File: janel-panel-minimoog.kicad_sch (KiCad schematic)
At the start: 2 parts, among them J2 Conn_01x03_Pin, J3 Conn_01x01_Pin

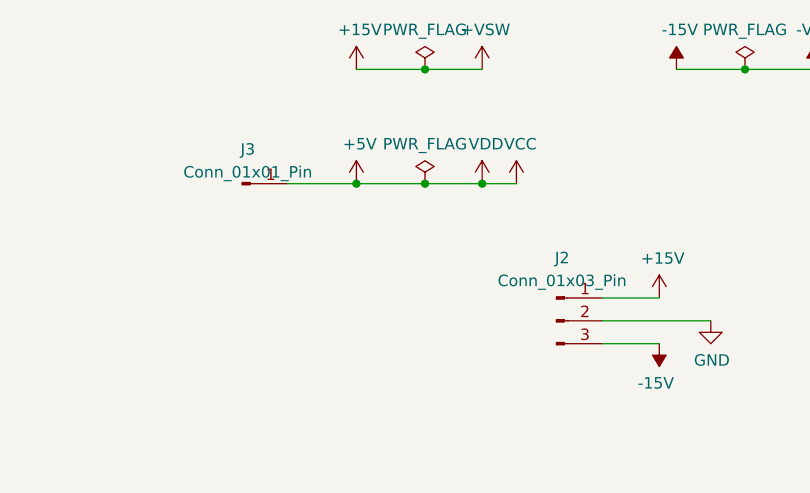
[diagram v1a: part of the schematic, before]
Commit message: Replace symbols with new library
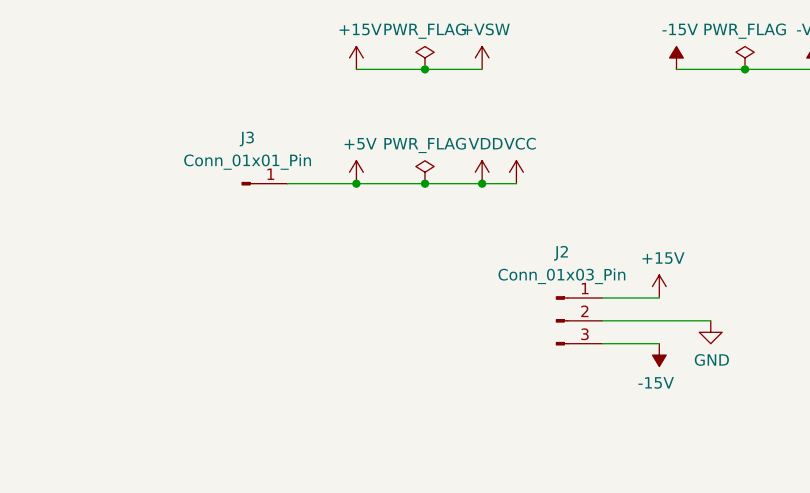
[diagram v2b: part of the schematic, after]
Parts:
- J2: footprint Connector_PinHeader_2.54mm:PinHeader_1x03_P2.54mm_Vertical -> (none)
- J3: footprint Connector_PinHeader_2.54mm:PinHeader_1x01_P2.54mm_Vertical -> (none)
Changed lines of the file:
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@@
 			)
 		)
-		(property "Description" ""
+		(property "Description" "Power symbol creates a global label with name \"+15V\""
 			(at 204.47 26.67 0)
 			(effects
@@
 					(size 1.27 1.27)
 				)
+				(hide yes)
 			)
 		)
@@
 			)
 		)
-		(property "Description" ""
+		(property "Description" "Power symbol creates a global label with name \"-15V\""
 			(at 240.03 26.67 0)
 			(effects
@@
 					(size 1.27 1.27)
 				)
+				(hide yes)
 			)
 		)
@@
 			)
 		)
-		(property "Description" ""
+		(property "Description" "Special symbol for telling ERC where power comes from"
 			(at 212.09 26.67 0)
 			(effects
@@
 					(size 1.27 1.27)
 				)
+				(hide yes)
 			)
 		)
@@
 			)
 		)
-		(property "Description" ""
+		(property "Description" "Special symbol for telling ERC where power comes from"
 			(at 247.65 26.67 0)
 			(effects
@@
 					(size 1.27 1.27)
 				)
+				(hide yes)
 			)
 		)
@@
 			)
 		)
-		(property "Description" ""
+		(property "Description" "Special symbol for telling ERC where power comes from"
 			(at 270.51 26.67 0)
 			(effects
@@
 					(size 1.27 1.27)
 				)
+				(hide yes)
 			)
 		)
@@
 			)
 		)
-		(property "Description" ""
+		(property "Description" "Power symbol creates a global label with name \"GND\" , ground"
 			(at 265.43 26.67 0)
 			(effects
@@
 					(size 1.27 1.27)
 				)
+				(hide yes)
 			)
 		)
@@
 			)
 		)
-		(property "Description" ""
+		(property "Description" "Power symbol creates a global label with name \"+VSW\""
 			(at 218.44 26.67 0)
 			(effects
@@
 					(size 1.27 1.27)
 				)
+				(hide yes)
 			)
 		)
@@
 			)
 		)
-		(property "Description" ""
+		(property "Description" "Power symbol creates a global label with name \"-VSW\""
 			(at 255.27 26.67 0)
 			(effects
@@
 					(size 1.27 1.27)
 				)
+				(hide yes)
 			)
 		)
@@
 			)
 		)
-		(property "Description" ""
+		(property "Description" "Power symbol creates a global label with name \"+5V\""
 			(at 204.47 39.37 0)
 			(effects
@@
 					(size 1.27 1.27)
 				)
+				(hide yes)
 			)
 		)
@@
 			)
 		)
-		(property "Description" ""
+		(property "Description" "Special symbol for telling ERC where power comes from"
 			(at 212.09 39.37 0)
 			(effects
@@
 					(size 1.27 1.27)
 				)
+				(hide yes)
 			)
 		)
@@
 			)
 		)
-		(property "Description" ""
+		(property "Description" "Power symbol creates a global label with name \"VDD\""
 			(at 218.44 39.37 0)
 			(effects
@@
 					(size 1.27 1.27)
 				)
+				(hide yes)
 			)
 		)
@@
 			)
 		)
-		(property "Description" ""
+		(property "Description" "Power symbol creates a global label with name \"VSS\""
 			(at 276.86 26.67 0)
 			(effects
@@
 					(size 1.27 1.27)
 				)
+				(hide yes)
 			)
 		)
@@
 			)
 		)
-		(property "Description" ""
+		(property "Description" "Power symbol creates a global label with name \"VCC\""
 			(at 222.25 39.37 0)
 			(effects
@@
 					(size 1.27 1.27)
 				)
+				(hide yes)
 			)
 		)
@@
 			)
 		)
-		(property "Description" ""
+		(property "Description" "Power symbol creates a global label with name \"GNDREF\" , reference supply ground"
 			(at 274.32 26.67 0)
 			(effects
@@
 					(size 1.27 1.27)
 				)
+				(hide yes)
 			)
 		)
@@
 			)
 		)
-		(property "Description" ""
+		(property "Description" "Power symbol creates a global label with name \"+15V\""
 			(at 238.125 52.07 0)
 			(effects
@@
 					(size 1.27 1.27)
 				)
+				(hide yes)
 			)
 		)
@@
 			)
 		)
-		(property "Description" ""
+		(property "Description" "Power symbol creates a global label with name \"-15V\""
 			(at 238.125 57.15 0)
 			(effects
@@
 					(size 1.27 1.27)
 				)
+				(hide yes)
 			)
 		)
@@
 		(fields_autoplaced yes)
 		(property "Reference" "J3"
-			(at 192.405 35.56 0)
+			(at 192.405 34.29 0)
 			(effects
 				(font
@@
 		)
 		(property "Value" "Conn_01x01_Pin"
-			(at 192.405 38.1 0)
-			(effects
-				(font
-					(size 1.27 1.27)
-				)
-			)
-		)
-		(property "Footprint" "Connector_PinHeader_2.54mm:PinHeader_1x01_P2.54mm_Vertical"
+			(at 192.405 36.83 0)
+			(effects
+				(font
+					(size 1.27 1.27)
+				)
+			)
+		)
+		(property "Footprint" ""
 			(at 191.77 39.37 0)
 			(effects
@@
 			)
 		)
-		(property "Description" ""
+		(property "Description" "Generic connector, single row, 01x01, script generated"
 			(at 191.77 39.37 0)
 			(effects
@@
 					(size 1.27 1.27)
 				)
+				(hide yes)
 			)
 		)
@@
 		(fields_autoplaced yes)
 		(property "Reference" "J2"
-			(at 227.33 47.625 0)
+			(at 227.33 46.99 0)
 			(effects
 				(font
@@
 		)
 		(property "Value" "Conn_01x03_Pin"
-			(at 227.33 50.165 0)
-			(effects
-				(font
-					(size 1.27 1.27)
-				)
-			)
-		)
-		(property "Footprint" "Connector_PinHeader_2.54mm:PinHeader_1x03_P2.54mm_Vertical"
+			(at 227.33 49.53 0)
+			(effects
+				(font
+					(size 1.27 1.27)
+				)
+			)
+		)
+		(property "Footprint" ""
 			(at 226.695 54.61 0)
 			(effects
@@
 			)
 		)
-		(property "Description" ""
+		(property "Description" "Generic connector, single row, 01x03, script generated"
 			(at 226.695 54.61 0)
 			(effects
@@
 					(size 1.27 1.27)
 				)
+				(hide yes)
 			)
 		)
@@
 			)
 		)
-		(property "Description" ""
+		(property "Description" "Power symbol creates a global label with name \"GND\" , ground"
 			(at 243.84 54.61 0)
 			(effects
@@
 					(size 1.27 1.27)
 				)
-			)
-		)
+				(hide yes)
+			)
+		)

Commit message: Label connectors, update footprints
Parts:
- J2: footprint (none) -> Connector_PinHeader_2.54mm:PinHeader_1x03_P2.54mm_Vertical
- J3: footprint (none) -> Connector_PinHeader_2.54mm:PinHeader_1x01_P2.54mm_Vertical
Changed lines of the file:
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@@
 			)
 		)
-		(property "Footprint" ""
+		(property "Footprint" "Connector_PinHeader_2.54mm:PinHeader_1x01_P2.54mm_Vertical"
 			(at 191.77 39.37 0)
 			(effects
@@
 			)
 		)
-		(property "Footprint" ""
+		(property "Footprint" "Connector_PinHeader_2.54mm:PinHeader_1x03_P2.54mm_Vertical"
 			(at 226.695 54.61 0)
 			(effects
